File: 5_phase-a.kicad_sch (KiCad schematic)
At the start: 28 parts, among them Q401 BSC072N08NS5, Q402 BSC072N08NS5, U401 IR2181S, U402 AD8418

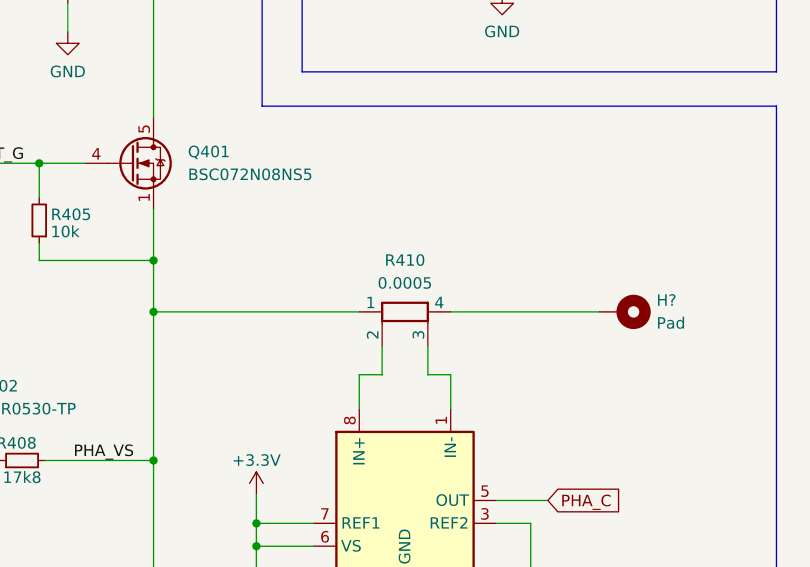
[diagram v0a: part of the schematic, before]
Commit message: chore: updated links and footprints
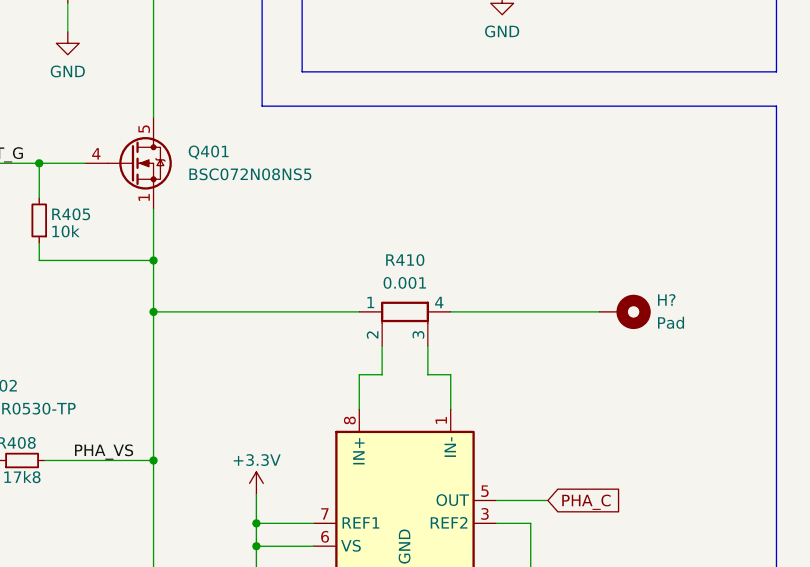
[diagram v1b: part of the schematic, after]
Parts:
- R410: value 0.0005 -> 0.001; footprint (none) -> Resistor_SMD:R_2512_6332Metric; Link (none) -> https://www.digikey.de/en/products/detail/bourns-inc/CSS2H-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
- U401: footprint (none) -> Package_SO:SOIC-8_3.9x4.9mm_P1.27mm; Link (none) -> https://www.digikey.de/en/products/detail/infineon-technolo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
- U402: footprint (none) -> Package_SO:SOIC-8_3.9x4.9mm_P1.27mm
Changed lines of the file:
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@@
       (effects (font (size 1.27 1.27)))
     )
-    (property "Value" "0.0005" (at 237.49 80.01 90)
-      (effects (font (size 1.27 1.27)))
-    )
-    (property "Footprint" "" (at 237.49 81.407 90)
+    (property "Value" "0.001" (at 237.49 80.01 90)
+      (effects (font (size 1.27 1.27)))
+    )
+    (property "Footprint" "Resistor_SMD:R_2512_6332Metric" (at 237.49 81.407 90)
       (effects (font (size 1.27 1.27)) hide)
     )
     (property "Datasheet" "~" (at 237.49 83.185 0)
+      (effects (font (size 1.27 1.27)) hide)
+    )
+    (property "Link" "https://www.digikey.de/en/products/detail/bourns-inc/CSS2H-2512R-1L00F/6023764" (at 237.49 83.185 90)
       (effects (font (size 1.27 1.27)) hide)
     )
@@
       (effects (font (size 1.27 1.27)) (justify left))
     )
-    (property "Footprint" "" (at 238.76 113.03 0)
+    (property "Footprint" "Package_SO:SOIC-8_3.9x4.9mm_P1.27mm" (at 238.76 113.03 0)
       (effects (font (size 1.27 1.27)) hide)
     )
@@
       (effects (font (size 1.27 1.27)) (justify left))
     )
-    (property "Footprint" "" (at 87.63 90.805 0)
+    (property "Footprint" "Package_SO:SOIC-8_3.9x4.9mm_P1.27mm" (at 87.63 90.805 0)
       (effects (font (size 1.27 1.27) italic) hide)
     )
@@
       (effects (font (size 1.27 1.27)) hide)
     )
+    (property "Link" "https://www.digikey.de/en/products/detail/infineon-technologies/IR2181SPBF/856520" (at 87.63 90.805 0)
+      (effects (font (size 1.27 1.27)) hide)
+    )

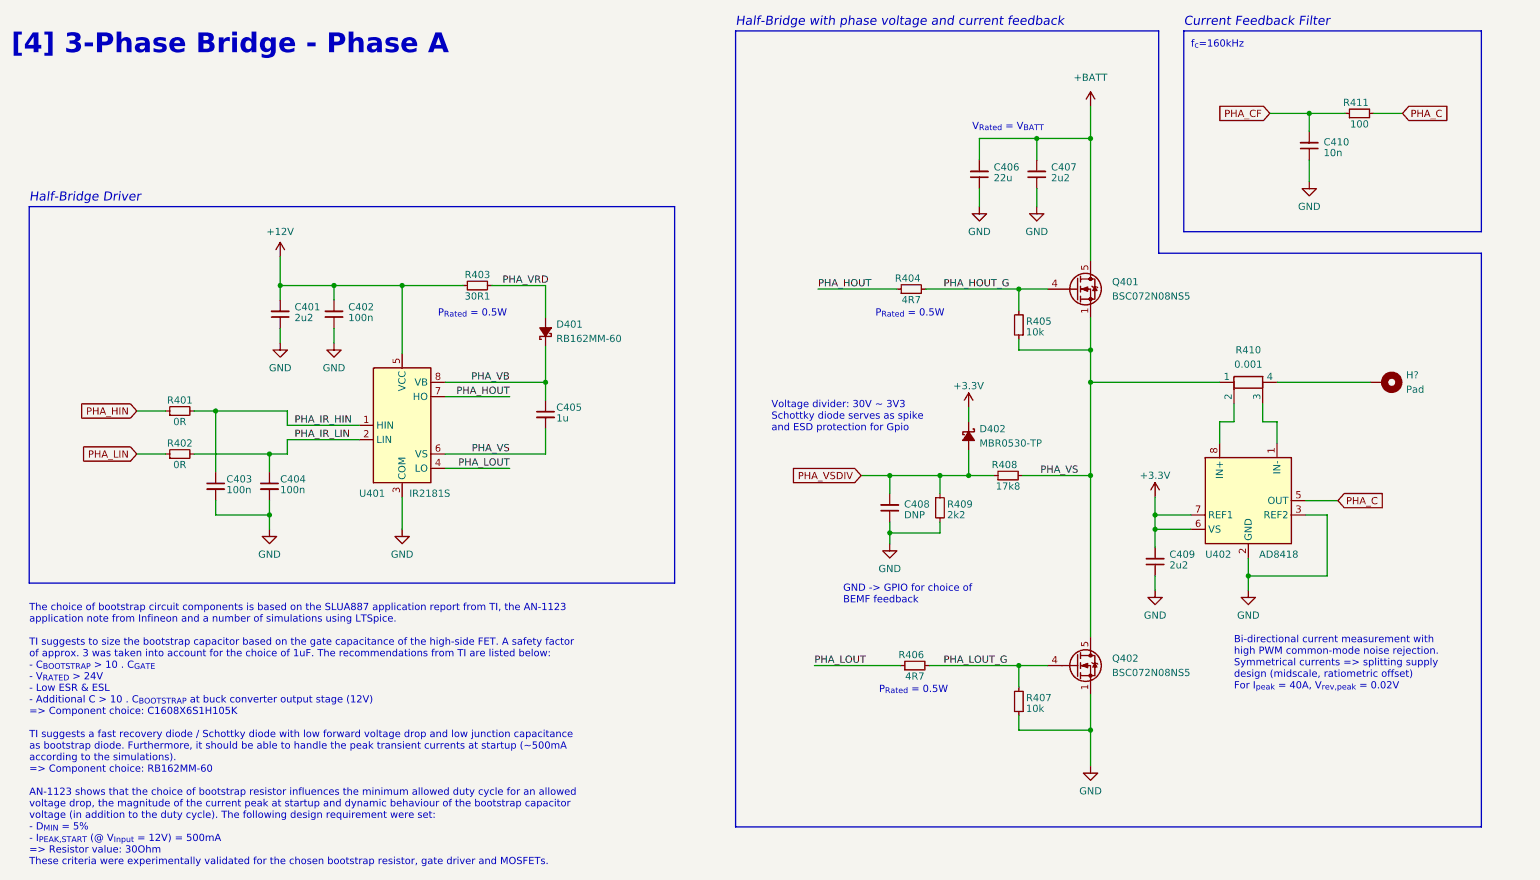
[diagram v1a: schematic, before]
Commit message: feat: new phases, LED pins
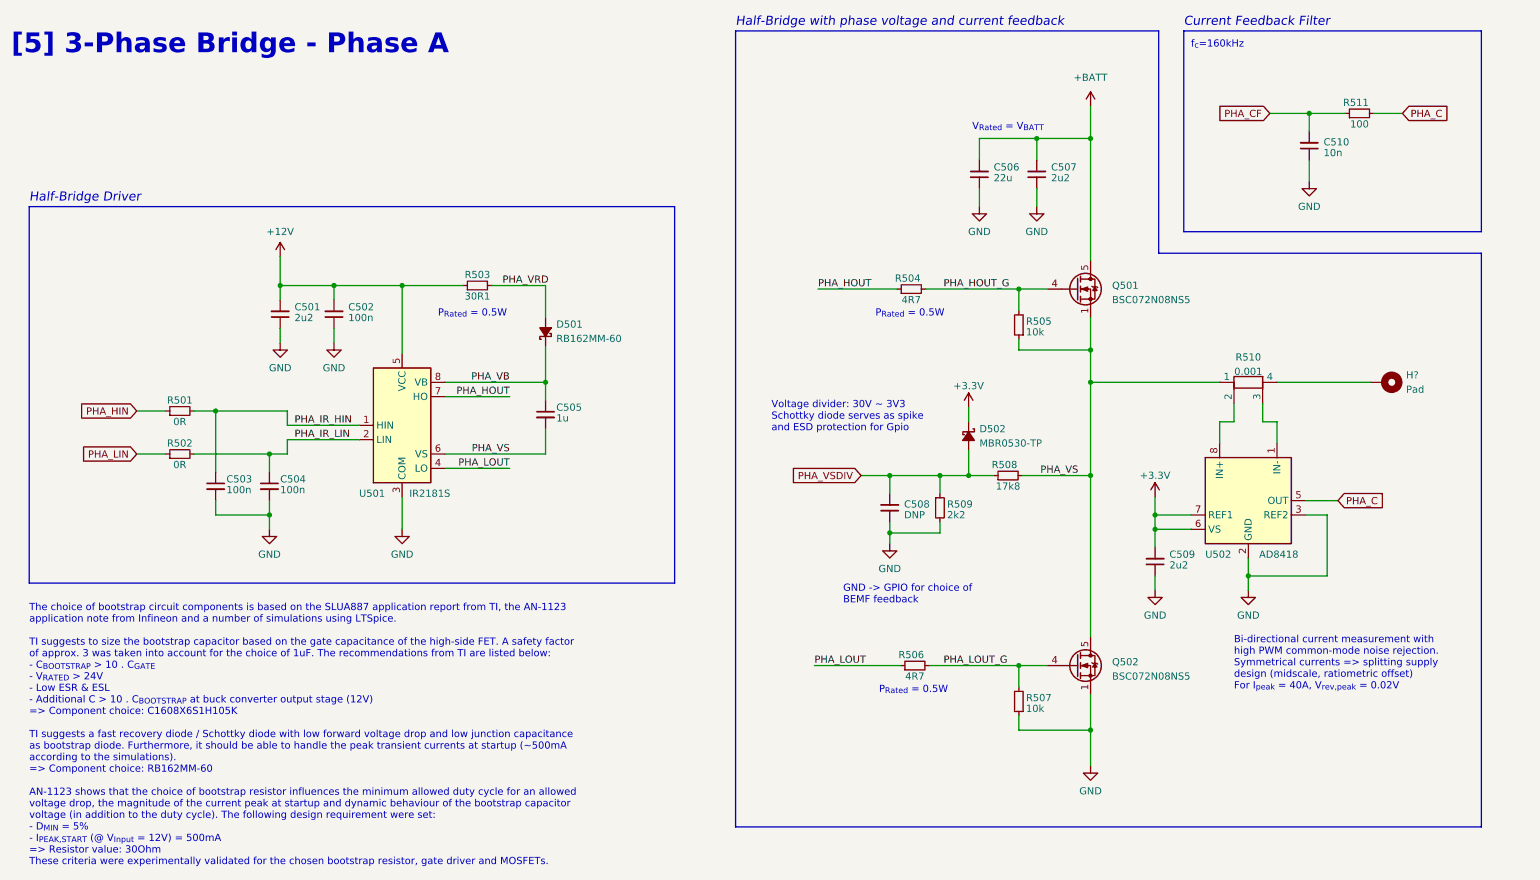
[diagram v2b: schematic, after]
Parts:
- R511: renamed from R411; footprint Resistor_SMD:R_0402_1005Metric_Pad0.72x0.64mm_HandSolder -> Resistor_SMD:R_0603_1608Metric_Pad0.98x0.95mm_HandSolder
- renumbered C401 to C501, C402 to C502, C403 to C503, C404 to C504, C405 to C505, C406 to C506, C407 to C507, C408 to C508, C409 to C509, C410 to C510, D401 to D501, D402 to D502, Q401 to Q501, Q402 to Q502, R401 to R501, R402 to R502, R403 to R503, R404 to R504, R405 to R505, R406 to R506, R407 to R507, R408 to R508, R409 to R509, R410 to R510, U401 to U501, U402 to U502
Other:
- note added: "[5] 3-Phase Bridge - Phase A"
- note removed: "[4] 3-Phase Bridge - Phase A"
- title: 3-Phase Bridge - Phase A [4] -> 3-Phase Bridge - Phase A

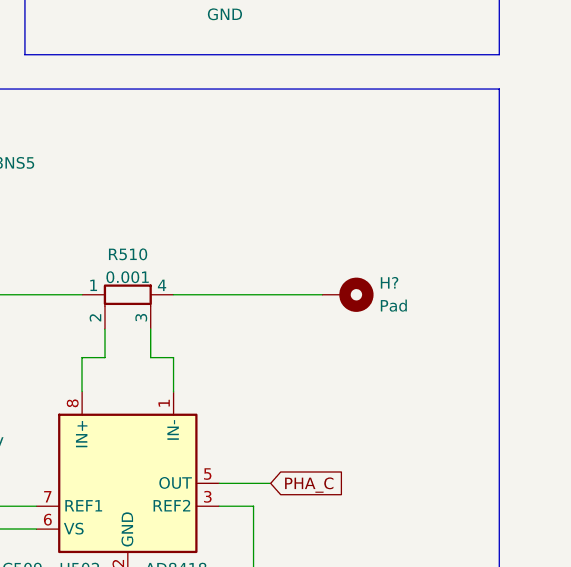
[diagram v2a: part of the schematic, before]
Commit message: feat: LED routing, encoder interface, footprint updates
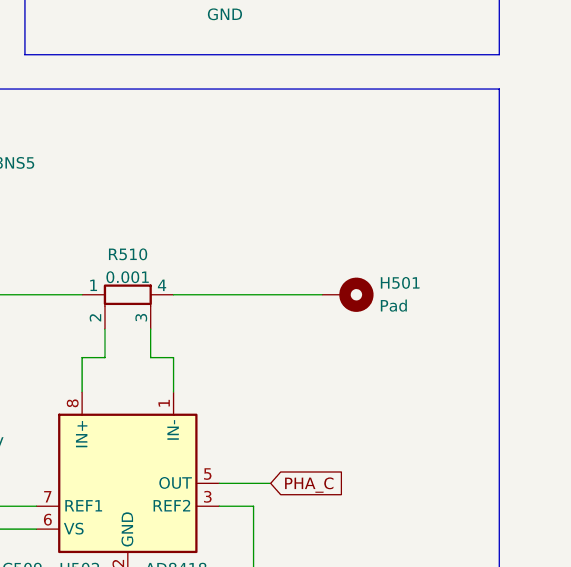
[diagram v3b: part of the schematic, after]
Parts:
- gave numbers to parts that had none: 1
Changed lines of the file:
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@@
   (title_block
     (title "3-Phase Bridge - Phase A")
-    (date "2023-04-16")
+    (date "2023-11-25")
     (rev "1.0")
   )
@@
   (symbol (lib_id "power:+3.3V") (at 187.96 87.63 0) (unit 1)
     (in_bom yes) (on_board yes) (dnp no)
-    (property "Reference" "#PWR?" (at 187.96 91.44 0)
+    (property "Reference" "#PWR0146" (at 187.96 91.44 0)
       (effects (font (size 1.27 1.27)) hide)
     )
@@
       (project "ESC_R1"
         (path "/9dea2e18-5867-4ed4-a12d-7ee109225de0/a82201a8-9dca-4a1d-828e-2de3fb3c1adb"
-          (reference "#PWR?") (unit 1)
+          (reference "#PWR0146") (unit 1)
         )
       )
@@
   (symbol (lib_id "power:GND") (at 189.865 52.07 0) (unit 1)
     (in_bom yes) (on_board yes) (dnp no)
-    (property "Reference" "#PWR?" (at 189.865 58.42 0)
+    (property "Reference" "#PWR0152" (at 189.865 58.42 0)
       (effects (font (size 1.27 1.27)) hide)
     )
@@
       (project "ESC_R1"
         (path "/9dea2e18-5867-4ed4-a12d-7ee109225de0/a82201a8-9dca-4a1d-828e-2de3fb3c1adb"
-          (reference "#PWR?") (unit 1)
+          (reference "#PWR0152") (unit 1)
         )
       )
@@
   (symbol (lib_id "Mechanical:MountingHole_Pad") (at 261.62 83.185 270) (unit 1)
     (in_bom yes) (on_board yes) (dnp no)
-    (property "Reference" "H?" (at 265.43 81.9149 90)
+    (property "Reference" "H501" (at 265.43 81.9149 90)
       (effects (font (size 1.27 1.27)) (justify left))
     )
@@
       (project "ESC_R1"
         (path "/9dea2e18-5867-4ed4-a12d-7ee109225de0/a82201a8-9dca-4a1d-828e-2de3fb3c1adb"
-          (reference "H?") (unit 1)
+          (reference "H501") (unit 1)
         )
       )
@@
   (symbol (lib_id "power:GND") (at 220.98 120.015 0) (unit 1)
     (in_bom yes) (on_board yes) (dnp no)
-    (property "Reference" "#PWR?" (at 220.98 126.365 0)
+    (property "Reference" "#PWR0144" (at 220.98 126.365 0)
       (effects (font (size 1.27 1.27)) hide)
     )
@@
       (project "ESC_R1"
         (path "/9dea2e18-5867-4ed4-a12d-7ee109225de0/a82201a8-9dca-4a1d-828e-2de3fb3c1adb"
-          (reference "#PWR?") (unit 1)
+          (reference "#PWR0144") (unit 1)
         )
       )
@@
   (symbol (lib_id "power:GND") (at 209.55 151.13 0) (unit 1)
     (in_bom yes) (on_board yes) (dnp no)
-    (property "Reference" "#PWR?" (at 209.55 157.48 0)
+    (property "Reference" "#PWR0145" (at 209.55 157.48 0)
       (effects (font (size 1.27 1.27)) hide)
     )
@@
       (project "ESC_R1"
         (path "/9dea2e18-5867-4ed4-a12d-7ee109225de0/a82201a8-9dca-4a1d-828e-2de3fb3c1adb"
-          (reference "#PWR?") (unit 1)
+          (reference "#PWR0145") (unit 1)
         )
       )
@@
   (symbol (lib_id "power:GND") (at 248.285 47.625 0) (unit 1)
     (in_bom yes) (on_board yes) (dnp no)
-    (property "Reference" "#PWR?" (at 248.285 53.975 0)
+    (property "Reference" "#PWR0149" (at 248.285 53.975 0)
       (effects (font (size 1.27 1.27)) hide)
     )
@@
       (project "ESC_R1"
         (path "/9dea2e18-5867-4ed4-a12d-7ee109225de0/a82201a8-9dca-4a1d-828e-2de3fb3c1adb"
-          (reference "#PWR?") (unit 1)
+          (reference "#PWR0149") (unit 1)
         )
       )
@@
   (symbol (lib_id "power:+BATT") (at 209.55 34.29 0) (unit 1)
     (in_bom yes) (on_board yes) (dnp no) (fields_autoplaced)
-    (property "Reference" "#PWR?" (at 209.55 38.1 0)
+    (property "Reference" "#PWR0150" (at 209.55 38.1 0)
       (effects (font (size 1.27 1.27)) hide)
     )
@@
       (project "ESC_R1"
         (path "/9dea2e18-5867-4ed4-a12d-7ee109225de0/a82201a8-9dca-4a1d-828e-2de3fb3c1adb"
-          (reference "#PWR?") (unit 1)
+          (reference "#PWR0150") (unit 1)
         )
       )
@@
   (symbol (lib_id "power:GND") (at 173.99 111.76 0) (unit 1)
     (in_bom yes) (on_board yes) (dnp no)
-    (property "Reference" "#PWR?" (at 173.99 118.11 0)
+    (property "Reference" "#PWR0148" (at 173.99 118.11 0)
       (effects (font (size 1.27 1.27)) hide)
     )
@@
       (project "ESC_R1"
         (path "/9dea2e18-5867-4ed4-a12d-7ee109225de0/a82201a8-9dca-4a1d-828e-2de3fb3c1adb"
-          (reference "#PWR?") (unit 1)
+          (reference "#PWR0148") (unit 1)
         )
       )
@@
   (symbol (lib_id "power:+3.3V") (at 220.98 103.505 0) (unit 1)
     (in_bom yes) (on_board yes) (dnp no)
-    (property "Reference" "#PWR?" (at 220.98 107.315 0)
+    (property "Reference" "#PWR0147" (at 220.98 107.315 0)
       (effects (font (size 1.27 1.27)) hide)
     )
@@
       (project "ESC_R1"
         (path "/9dea2e18-5867-4ed4-a12d-7ee109225de0/a82201a8-9dca-4a1d-828e-2de3fb3c1adb"
-          (reference "#PWR?") (unit 1)
+          (reference "#PWR0147") (unit 1)
         )
       )
@@
   (symbol (lib_id "power:GND") (at 200.025 52.07 0) (unit 1)
     (in_bom yes) (on_board yes) (dnp no)
-    (property "Reference" "#PWR?" (at 200.025 58.42 0)
+    (property "Reference" "#PWR0151" (at 200.025 58.42 0)
       (effects (font (size 1.27 1.27)) hide)
     )
@@
       (project "ESC_R1"
         (path "/9dea2e18-5867-4ed4-a12d-7ee109225de0/a82201a8-9dca-4a1d-828e-2de3fb3c1adb"
-          (reference "#PWR?") (unit 1)
+          (reference "#PWR0151") (unit 1)
         )
       )
@@
   (symbol (lib_id "power:GND") (at 237.49 120.015 0) (unit 1)
     (in_bom yes) (on_board yes) (dnp no)
-    (property "Reference" "#PWR?" (at 237.49 126.365 0)
+    (property "Reference" "#PWR0143" (at 237.49 126.365 0)
       (effects (font (size 1.27 1.27)) hide)
     )
@@
       (project "ESC_R1"
         (path "/9dea2e18-5867-4ed4-a12d-7ee109225de0/a82201a8-9dca-4a1d-828e-2de3fb3c1adb"
-          (reference "#PWR?") (unit 1)
-        )
-      )
+          (reference "#PWR0143") (unit 1)
+        )
+      )

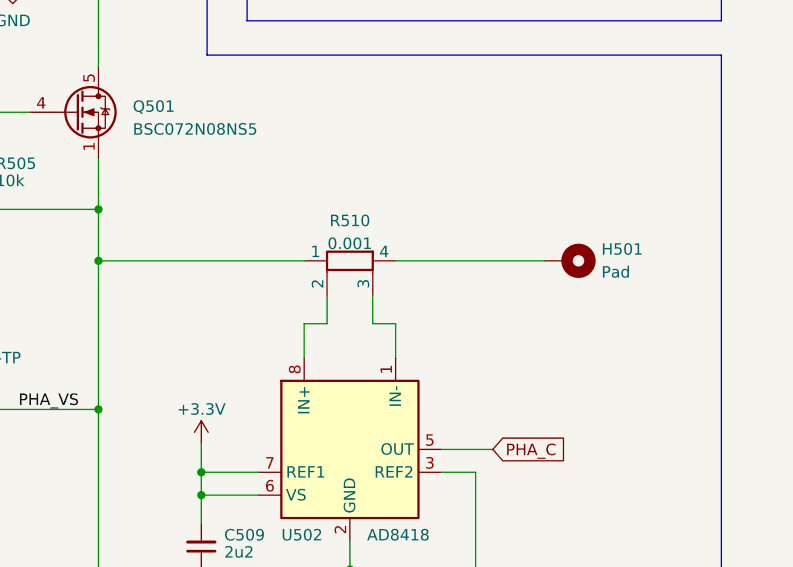
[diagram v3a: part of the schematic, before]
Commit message: feat: footprint assignment, circuit check and routing kickoff
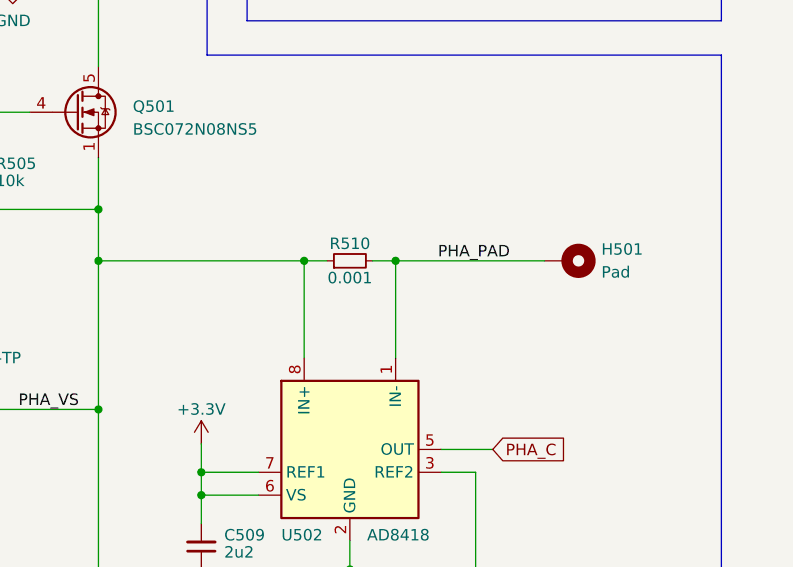
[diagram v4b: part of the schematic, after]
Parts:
- removed R510: 0.001, Resistor_SMD:R_2512_6332Metric, symbol Device:R_Shunt
- added R510: 0.001, Resistor_SMD:R_1206_3216Metric_Pad1.30x1.75mm_HandSolder, symbol Device:R_Small
- C510: footprint Capacitor_SMD:C_0402_1005Metric_Pad0.74x0.62mm_HandSolder -> Capacitor_SMD:C_0603_1608Metric_Pad1.08x0.95mm_HandSolder
- D501: Link (none) -> https://www.digikey.de/en/products/detail/rohm-semiconducto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
- D502: Link (none) -> https://www.digikey.de/en/products/detail/micro-commercial-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
- H501: footprint (none) -> TestPoint:TestPoint_THTPad_4.0x4.0mm_Drill2.0mm
- Q501, Q502: Link (none) -> https://www.digikey.de/en/products/detail/infineon-technolo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
- R508, R509: footprint Resistor_SMD:R_0402_1005Metric_Pad0.72x0.64mm_HandSolder -> Resistor_SMD:R_0603_1608Metric_Pad0.98x0.95mm_HandSolder
- U502: Link (none) -> https://www.digikey.de/en/products/detail/analog-devices-in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
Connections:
- net PHA_VS: now also U502.8 (IN+), R510.1
- net PHA_PAD: now reaches U502.1 (IN-)
- net PHA_PAD: now also H501.1, R510.2
